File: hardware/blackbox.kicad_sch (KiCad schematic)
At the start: 3 parts, among them U13 PY25Q128HA-DFH-IR

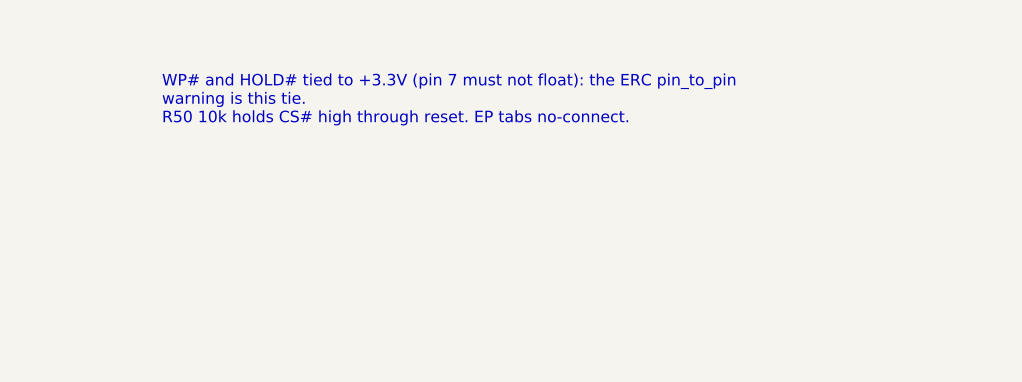
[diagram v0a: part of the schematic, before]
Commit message: Correct Whoop schematic and prepare component library for routing
Add local BMI270 bypassing, improve regulator capacitance margin, isolate
bidirectional DShot supply domains, and correct PA reference accuracy.
Remove Q28/R11 with matching firmware polarity and retain the proven
OpenFC-Lite OSD topology. Correct the receiver LED bypass rail.

Synchronize PCB connectivity, verify component pins and land patterns,
and provide firmware bindings plus placement/layer guidance. Replace stale
manual BOM and interface plans with schematic-derived exports.

Validation: ERC 0, seven netlist checks, 48 footprint checks, 22 rule
behavior cases, and PCB schematic parity 0. The parked PCB retains layout
DRC findings and 499 unconnected items; no manufacturing or flight release.
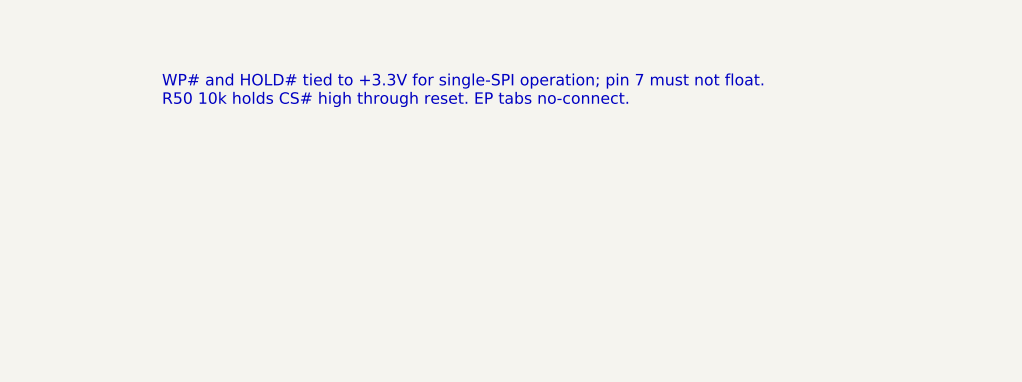
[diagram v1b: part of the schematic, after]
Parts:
- U13: symbol lib:PY25Q128HA-DFH-IR -> lib:PY25Q128HA-DFH-IR_SPI
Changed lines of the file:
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@@
 		)
 	)
-	(text_box "WP# and HOLD# tied to +3.3V (pin 7 must not float): the ERC pin_to_pin warning is this tie.\nR50 10k holds CS# high through reset. EP tabs no-connect."
+	(text_box "WP# and HOLD# tied to +3.3V for single-SPI operation; pin 7 must not float.\nR50 10k holds CS# high through reset. EP tabs no-connect."
 		(exclude_from_sim no)
 		(at 118.11 21.59 0)
@@
 	)
 	(symbol
-		(lib_id "lib:PY25Q128HA-DFH-IR")
+		(lib_id "lib:PY25Q128HA-DFH-IR_SPI")
 		(at 76.2 68.58 0)
 		(unit 1)
